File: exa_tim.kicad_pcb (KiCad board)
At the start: 4 copper layers, 42 x 42 mm, 54 parts, among them J1 Conn_ARM_JTAG_SWD_10, J2 FH12A-24S-0.5SH(55), Q1 SI2333DS-T1-E3, Q2 DMN3067LW-7, SW1 SKHLLFA010, SW2 SKHLLFA010, SW3 SKHLLFA010, SW4 SKHLLFA010, U1 STM32L071KZUx, U2 CAM-M8C-0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

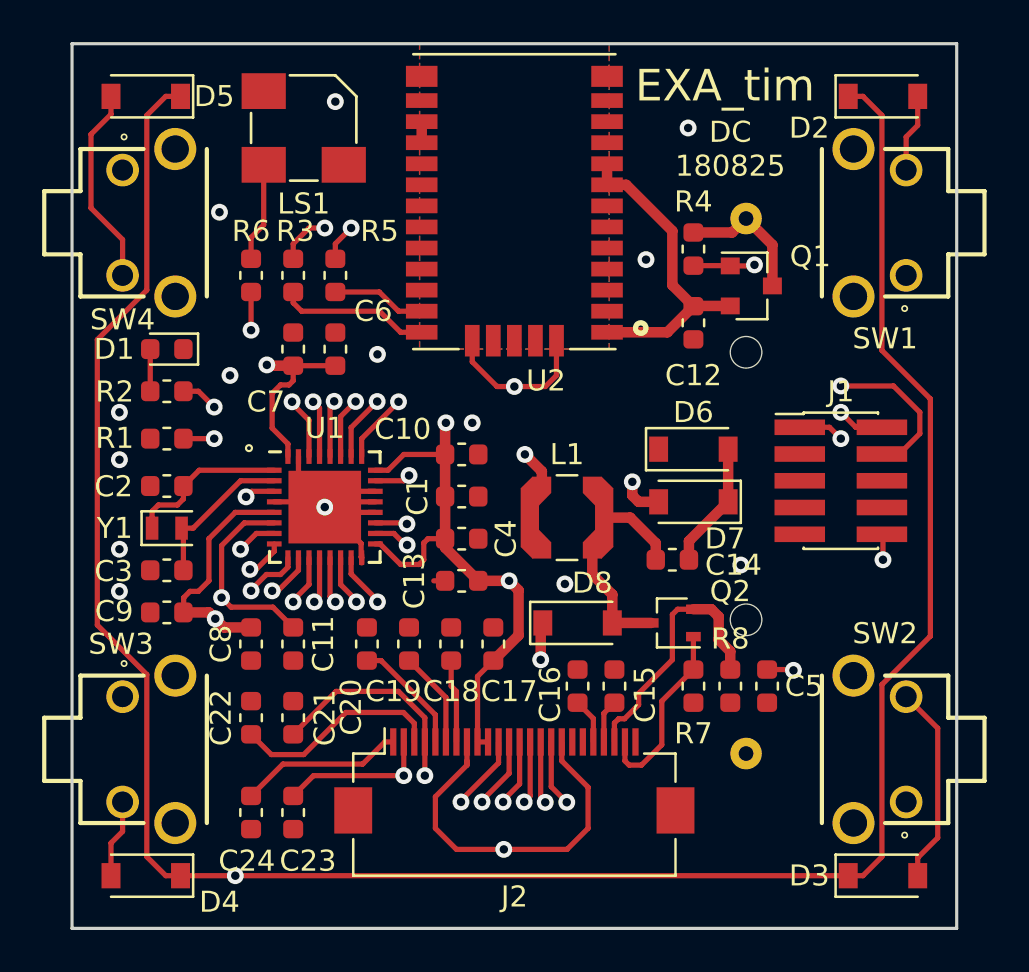
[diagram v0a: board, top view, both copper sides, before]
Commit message: Changed epaper connection to bottom feeding
Switched from FH12A to FH12, which is bottom feeding. This way the
PCB doesn't need to be mounted with the top facing down.

Also moved the battery now back to the original version. Hopefully
the battery will fit properly.
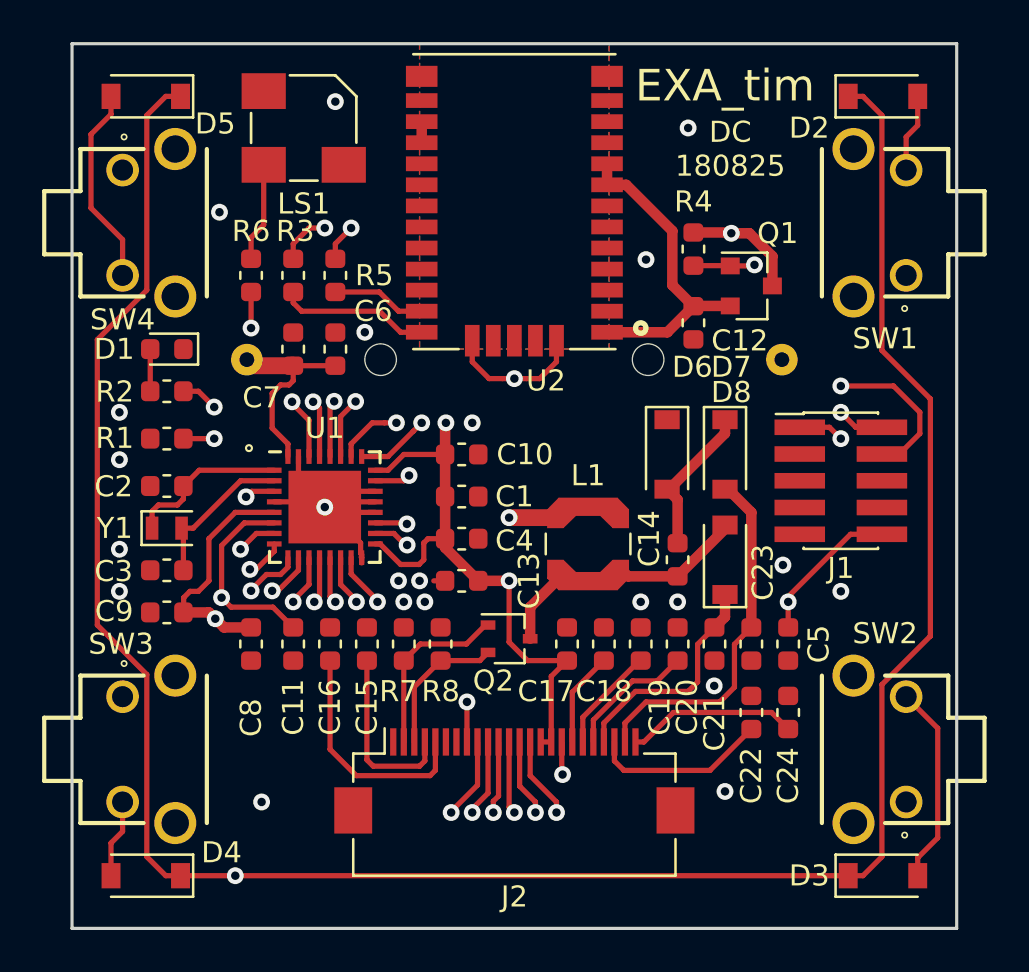
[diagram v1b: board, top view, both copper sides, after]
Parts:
- J2: value FH12A-24S-0.5SH(55) -> FH12-24S-0.5SH(55)
- moved C24 25.9 mm to (134.0, 101.8), turned to 90 degrees
- moved C22 23.8 mm to (132.2, 101.8)
- moved C23 23.2 mm to (132.2, 98.5)
- moved C21 20.3 mm to (130.5, 98.5), turned to 270 degrees
- moved C20 14.8 mm to (128.8, 98.5)
- moved R7 13.9 mm to (115.8, 98.5), turned to 90 degrees
- moved R8 13.9 mm to (117.5, 98.5), turned to 90 degrees
- moved C15 11.9 mm to (114.0, 98.5)
- moved C16 11.9 mm to (112.2, 98.5)
- moved C19 11.0 mm to (127.0, 98.5)
- moved Q2 7.79 mm to (120.8, 98.2), turned to 0 degrees
- moved D8 7.62 mm to (131.0, 94.5), turned to 90 degrees
- moved C18 7.25 mm to (125.2, 98.5)
- moved BT1 3.54 mm to (121.0, 93.5), turned to 180 degrees
- moved C17 3.50 mm to (123.5, 98.5)
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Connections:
- J2 pad 1: Net-(C24-Pad1) -> Net-(J2-Pad1)
- J2 pad 10: 3V -> /RESET
- J2 pad 11: /MOSI -> /DC
- J2 pad 12: /SCK -> /CS
- J2 pad 13: /CS -> /SCK
- J2 pad 14: /DC -> /MOSI
- J2 pad 15: /RESET -> 3V
- J2 pad 16: /BUSY -> 3V
- J2 pad 18: Net-(J2-Pad18) -> Net-(C18-Pad1)
- J2 pad 19: Net-(J2-Pad19) -> Net-(C19-Pad1)
- J2 pad 2: /PREVGL -> /GDR
- J2 pad 20: Net-(C16-Pad2) -> Net-(C20-Pad1)
- J2 pad 21: Net-(C15-Pad1) -> /PREVGH
- J2 pad 22: /RESE -> Net-(C22-Pad1)
- J2 pad 23: /GDR -> /PREVGL
- J2 pad 24: Net-(J2-Pad24) -> Net-(C24-Pad1)
- J2 pad 3: Net-(C22-Pad1) -> /RESE
- J2 pad 4: /PREVGH -> Net-(C15-Pad1)
- J2 pad 5: Net-(C20-Pad1) -> Net-(C16-Pad2)
- J2 pad 6: Net-(C19-Pad1) -> Net-(J2-Pad6)
- J2 pad 7: Net-(C18-Pad1) -> Net-(J2-Pad7)
- J2 pad 9: 3V -> /BUSY
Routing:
- net GND: track 43.3 -> 28.3 mm, vias 15 -> 24
- net /PREVGL: track 27.7 -> 17.1 mm, vias 2 -> 0
- net /PREVGH: track 19.9 -> 10.8 mm, vias 2 -> 0
- net Net-(C16-Pad2): track 2.17 -> 11.2 mm
- net /SCK: track 19.0 -> 26.4 mm
- net /NRST: track 52.8 -> 60.1 mm, vias 3 -> 2
- net /MOSI: track 19.9 -> 26.5 mm
- net Net-(C15-Pad1): track 2.07 -> 8.59 mm
- net /RESE: track 12.5 -> 6.92 mm
- net /DC: track 18.2 -> 22.2 mm
- net /CS: track 23.2 -> 19.6 mm
- net /BTN2: track 45.0 -> 46.9 mm
- net /RESET: track 18.4 -> 20.1 mm
- net Net-(C22-Pad1): track 10.1 -> 8.40 mm
- net 3V: track 212.2 -> 213.7 mm
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
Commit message: Rework PCP for more compact size
I reworked the PCB layout to archive a more compact
PCB layout / size. This should make the construction of
the watch casing much more easier.

Maybe we need to change the switches for a more fitting
design (maybe SMD mounted switches).
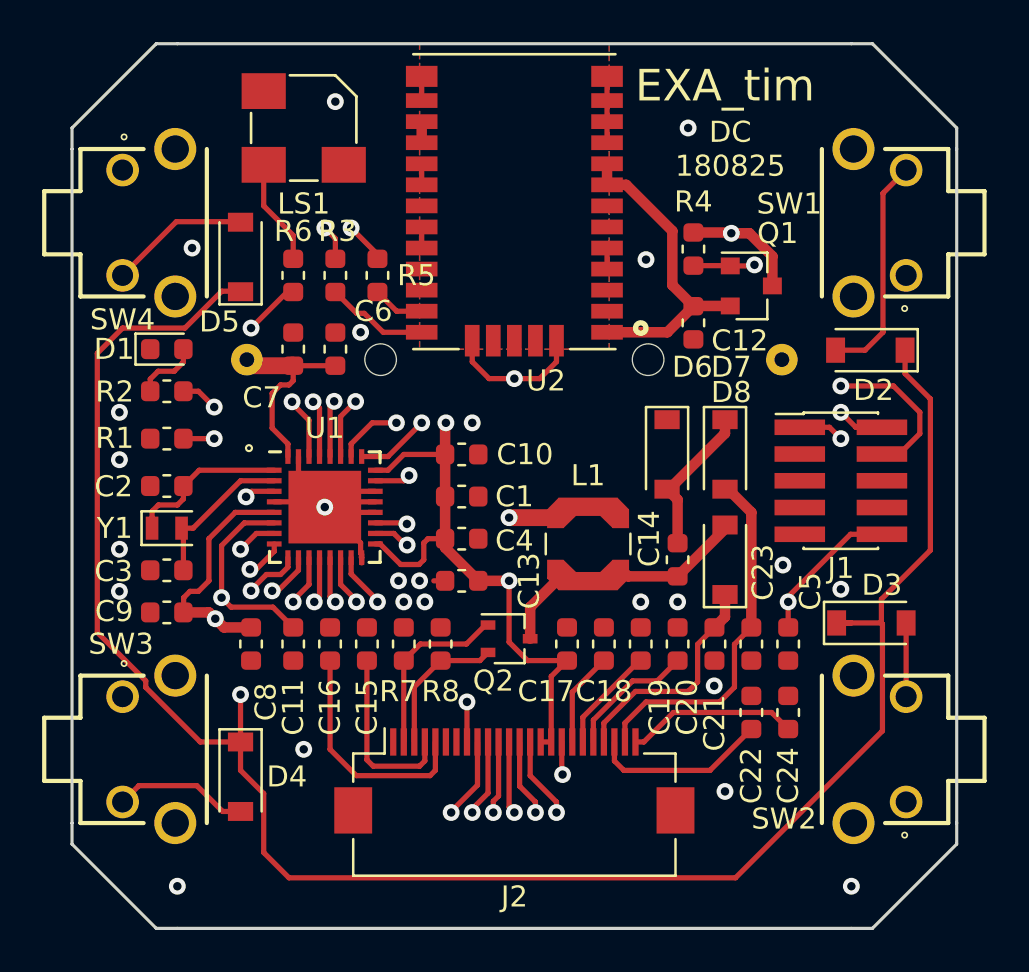
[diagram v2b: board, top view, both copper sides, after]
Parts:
- moved D2 12.1 mm to (137.9, 84.5), turned to 180 degrees
- moved D3 12.0 mm to (137.9, 97.5)
- moved D5 8.85 mm to (108.0, 80.1), turned to 90 degrees
- moved D4 6.51 mm to (108.0, 104.8), turned to 270 degrees
- moved R3 2.00 mm to (110.5, 81.0)
- moved R5 2.00 mm to (114.5, 81.0)
- moved R6 2.00 mm to (112.5, 81.0)
- turned D1 to 0 degrees
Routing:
- net /WKUP1: track 136.7 -> 107.9 mm
- net GND: track 28.3 -> 35.6 mm, vias 24 -> 26
- net /BTN1: track 36.7 -> 43.7 mm
- net /BTN2: track 46.9 -> 40.3 mm
- net 3V: track 213.7 -> 209.7 mm
- net /BTN4: track 25.7 -> 22.8 mm
- net /BTN3: track 36.0 -> 38.5 mm
- net /RX_GNSS: track 7.19 -> 4.89 mm
- net /TX_GNSS: track 4.48 -> 2.48 mm
- net Net-(D1-Pad2): track 2.00 -> 3.10 mm
- net /ALARM: track 16.4 -> 17.4 mm
- net /TX: track 25.0 -> 24.2 mm
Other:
- outline, holes or cut-outs redrawn

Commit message: Change battery to CR2032 for better height profile
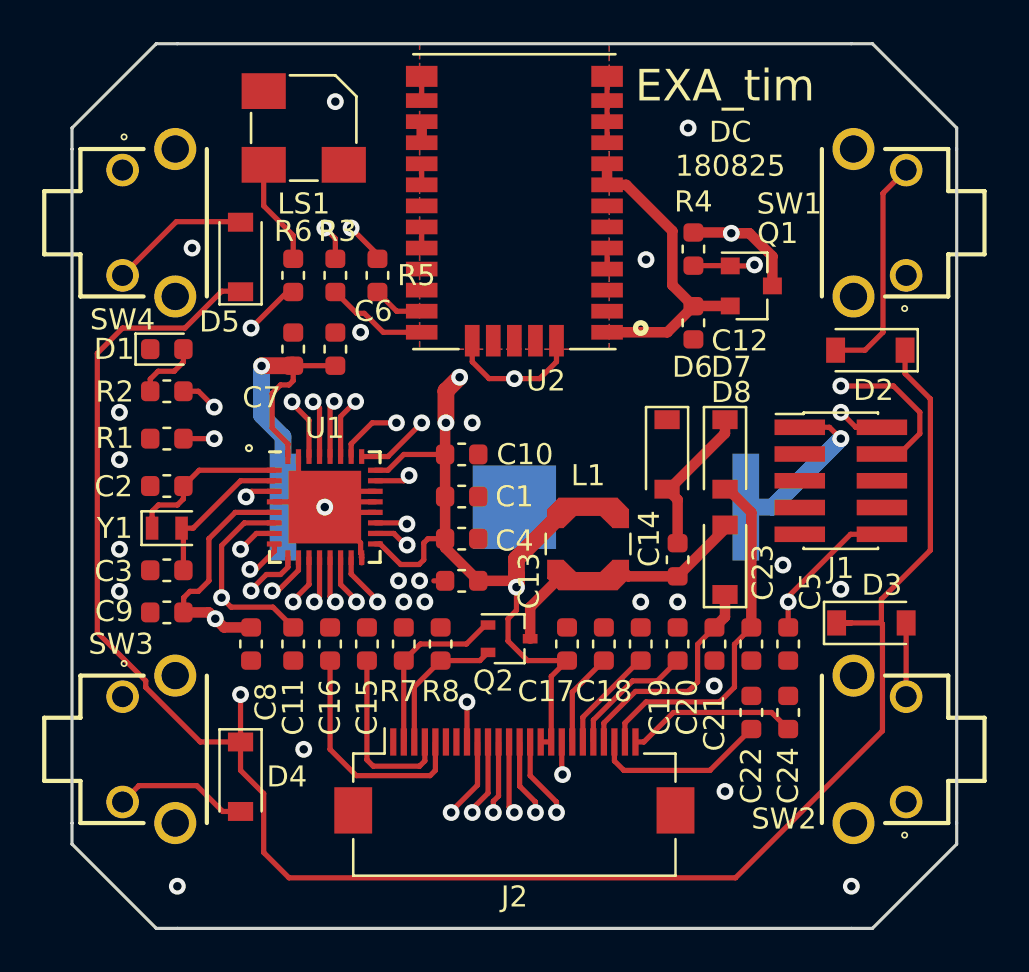
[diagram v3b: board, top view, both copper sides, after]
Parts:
- BT1: value NL5077-LF -> 3034TR; footprint exa_tim:NL5077-LF -> exa_tim:BatteryHolder_Keystone_3034_1x20mm
- moved BT1 1.50 mm to (121.0, 92.0)
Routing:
- net 3V: track 209.7 -> 226.2 mm, vias 6 -> 7
- net /GNSS_EN: track 39.1 -> 40.9 mm

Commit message: Use different buttons to get thinner design
I used other buttons and relocated the buttons and the
SWD connector to the bottom of the PCB to get a much
thinner design. PCB will use a 1mm board.
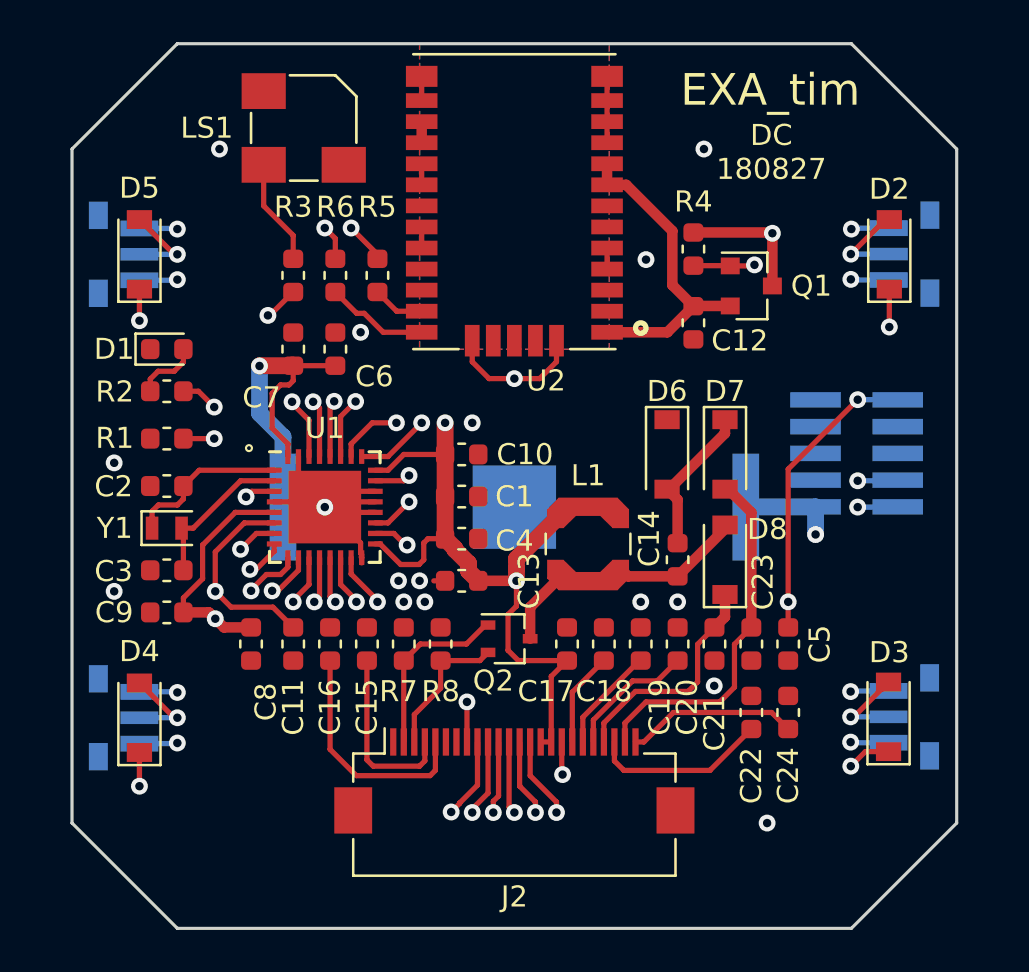
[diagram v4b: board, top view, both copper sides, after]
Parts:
- J1: value Conn_ARM_JTAG_SWD_10 -> 20021121-00010C4LF; footprint Connector_PinHeader_1.27mm:PinHeader_2x05_P1.27mm_Vertical_SMD -> exa_tim:PinHeader_2x05_P1.27mm_Vertical_SMD; moved to B.Cu
- SW1, SW2, SW3, SW4: value SKHLLFA010 -> SKRTLBE010; footprint exa_tim:SKHLLFA010 -> exa_tim:SKRTLBE010; moved to B.Cu
- moved D4 5.56 mm to (103.2, 102.0), turned to 90 degrees
- moved D5 4.80 mm to (103.2, 80.0)
- moved D2 4.64 mm to (138.8, 80.0), turned to 90 degrees
- moved D3 4.53 mm to (138.8, 102.0), turned to 90 degrees
- moved SW2 2.47 mm to (139.7, 102.0), turned to 270 degrees
- moved SW1 2.43 mm to (139.7, 80.0), turned to 270 degrees
- moved SW3 2.42 mm to (102.3, 102.0), turned to 90 degrees
- moved SW4 2.42 mm to (102.3, 80.0), turned to 90 degrees
- moved J1 1.50 mm to (137.2, 89.5)
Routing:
- net /NRST: track 60.1 -> 44.5 mm, vias 2 -> 3
- net /BTN1: track 43.7 -> 34.5 mm, vias 1 -> 2
- net /CS: track 19.6 -> 27.6 mm
- net 3V: track 226.2 -> 218.7 mm, vias 7 -> 14
- net /BTN3: track 38.5 -> 32.0 mm, vias 1 -> 2
- net /WKUP1: track 107.9 -> 101.5 mm, vias 2 -> 5
- net /GNSS_EN: track 40.9 -> 34.5 mm
- net /BTN4: track 22.8 -> 16.7 mm, vias 1 -> 2
- net /SCK: track 26.0 -> 31.6 mm
- net /SWCLK: track 31.6 -> 27.1 mm
- net /SWDIO: track 25.7 -> 26.9 mm
- net /RX: track 29.2 -> 29.9 mm
- net /BTN2: track 40.3 -> 40.6 mm, vias 1 -> 2
- net GND: vias 26 -> 18
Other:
- outline, holes or cut-outs redrawn
- board text added: "DC 180827"
- board text removed: "DC 180825"
